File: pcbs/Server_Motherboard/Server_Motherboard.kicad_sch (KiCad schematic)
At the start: 18 parts, among them J1 GSB1C41110SSHR, J2 Conn_01x20, J3 Conn_01x20, U1 ESP32-C3-MINI-1-H4X

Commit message: moving imported parts from my global dir to within this repo
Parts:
- added IC21: DRV8210DRLR, SOTFL50P160X60-6N, symbol SamacSys_Parts:DRV8210DRLR
- added U2: MCP23S17_ML, Package_DFN_QFN:QFN-28-1EP_6x6mm_P0.65mm_EP4.25x4.25mm, symbol Interface_Expansion:MCP23S17_ML
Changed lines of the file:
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@@
+    )
+  )
+  (symbol (lib_id "Interface_Expansion:MCP23S17_ML") (at 250.19 153.67 0) (unit 1)
+    (in_bom yes) (on_board yes) (dnp no) (fields_autoplaced)
+    (property "Reference" "U2" (at 252.3841 125.73 0)
+      (effects (font (size 1.27 1.27)) (justify left))
+    )
+    (property "Value" "MCP23S17_ML" (at 252.3841 128.27 0)
+      (effects (font (size 1.27 1.27)) (justify left))
+    )
+    (property "Footprint" "Package_DFN_QFN:QFN-28-1EP_6x6mm_P0.65mm_EP4.25x4.25mm" (at 255.27 179.07 0)
+      (effects (font (size 1.27 1.27)) (justify left) hide)
+    )
+    (property "Datasheet" "http://ww1.microchip.com/downloads/en/DeviceDoc/20001952C.pdf" (at 255.27 181.61 0)
+      (effects (font (size 1.27 1.27)) (justify left) hide)
+    )
+    (pin "15")
+    (pin "27")
+    (pin "7")
+    (pin "12")
+    (pin "3")
+    (pin "26")
+    (pin "10")
+    (pin "18")
+    (pin "25")
+    (pin "1")
+    (pin "13")
+    (pin "16")
+    (pin "14")
+    (pin "22")
+    (pin "28")
+    (pin "6")
+    (pin "8")
+    (pin "24")
+    (pin "11")
+    (pin "20")
+    (pin "2")
+    (pin "21")
+    (pin "29")
+    (pin "23")
+    (pin "4")
+    (pin "9")
+    (pin "5")
+    (pin "17")
+    (pin "19")
+    (instances
+      (project "Server_Motherboard"
+        (path "/2e2729a6-36ba-49a4-8404-024e36daa1b6"
+          (reference "U2") (unit 1)
+        )
+      )
     )
   )
@@
         )
       )
+    )
+  )
+  (symbol (lib_id "SamacSys_Parts:DRV8210DRLR") (at 189.23 144.78 0) (unit 1)
+    (in_bom yes) (on_board yes) (dnp no) (fields_autoplaced)
+    (property "Reference" "IC21" (at 203.2 137.16 0)
+      (effects (font (size 1.27 1.27)))
+    )
+    (property "Value" "DRV8210DRLR" (at 203.2 139.7 0)
+      (effects (font (size 1.27 1.27)))
+    )
+    (property "Footprint" "SOTFL50P160X60-6N" (at 213.36 142.24 0)
+      (effects (font (size 1.27 1.27)) (justify left) hide)
+    )
+    (property "Datasheet" "https://www.ti.com/lit/ds/symlink/drv8210.pdf?ts=1641207817417&ref_url=https%253A%252F%252Fwww.google.com%252F" (at 213.36 144.78 0)
+      (effects (font (size 1.27 1.27)) (justify left) hide)
+    )
+    (property "Description" "Motor / Motion / Ignition Controllers & Drivers 12-V, 1.76-A brushed DC motor driver with auto sleep mode" (at 213.36 147.32 0)
+      (effects (font (size 1.27 1.27)) (justify left) hide)
+    )
+    (property "Height" "0.6" (at 213.36 149.86 0)
+      (effects (font (size 1.27 1.27)) (justify left) hide)
+    )
+    (property "Mouser Part Number" "595-DRV8210DRLR" (at 213.36 152.4 0)
+      (effects (font (size 1.27 1.27)) (justify left) hide)
+    )
+    (property "Mouser Price/Stock" "https://www.mouser.co.uk/ProductDetail/Texas-Instruments/DRV8210DRLR?qs=7D1LtPJG0i1B1CHsXZuruQ%3D%3D" (at 213.36 154.94 0)
+      (effects (font (size 1.27 1.27)) (justify left) hide)
+    )
+    (property "Manufacturer_Name" "Texas Instruments" (at 213.36 157.48 0)
+      (effects (font (size 1.27 1.27)) (justify left) hide)
+    )
+    (property "Manufacturer_Part_Number" "DRV8210DRLR" (at 213.36 160.02 0)
+      (effects (font (size 1.27 1.27)) (justify left) hide)
+    )
+    (pin "4")
+    (pin "5")
+    (pin "1")
+    (pin "3")
+    (pin "6")
+    (pin "2")
+    (instances
+      (project "Server_Motherboard"
+        (path "/2e2729a6-36ba-49a4-8404-024e36daa1b6"
+          (reference "IC21") (unit 1)
+        )
+      )

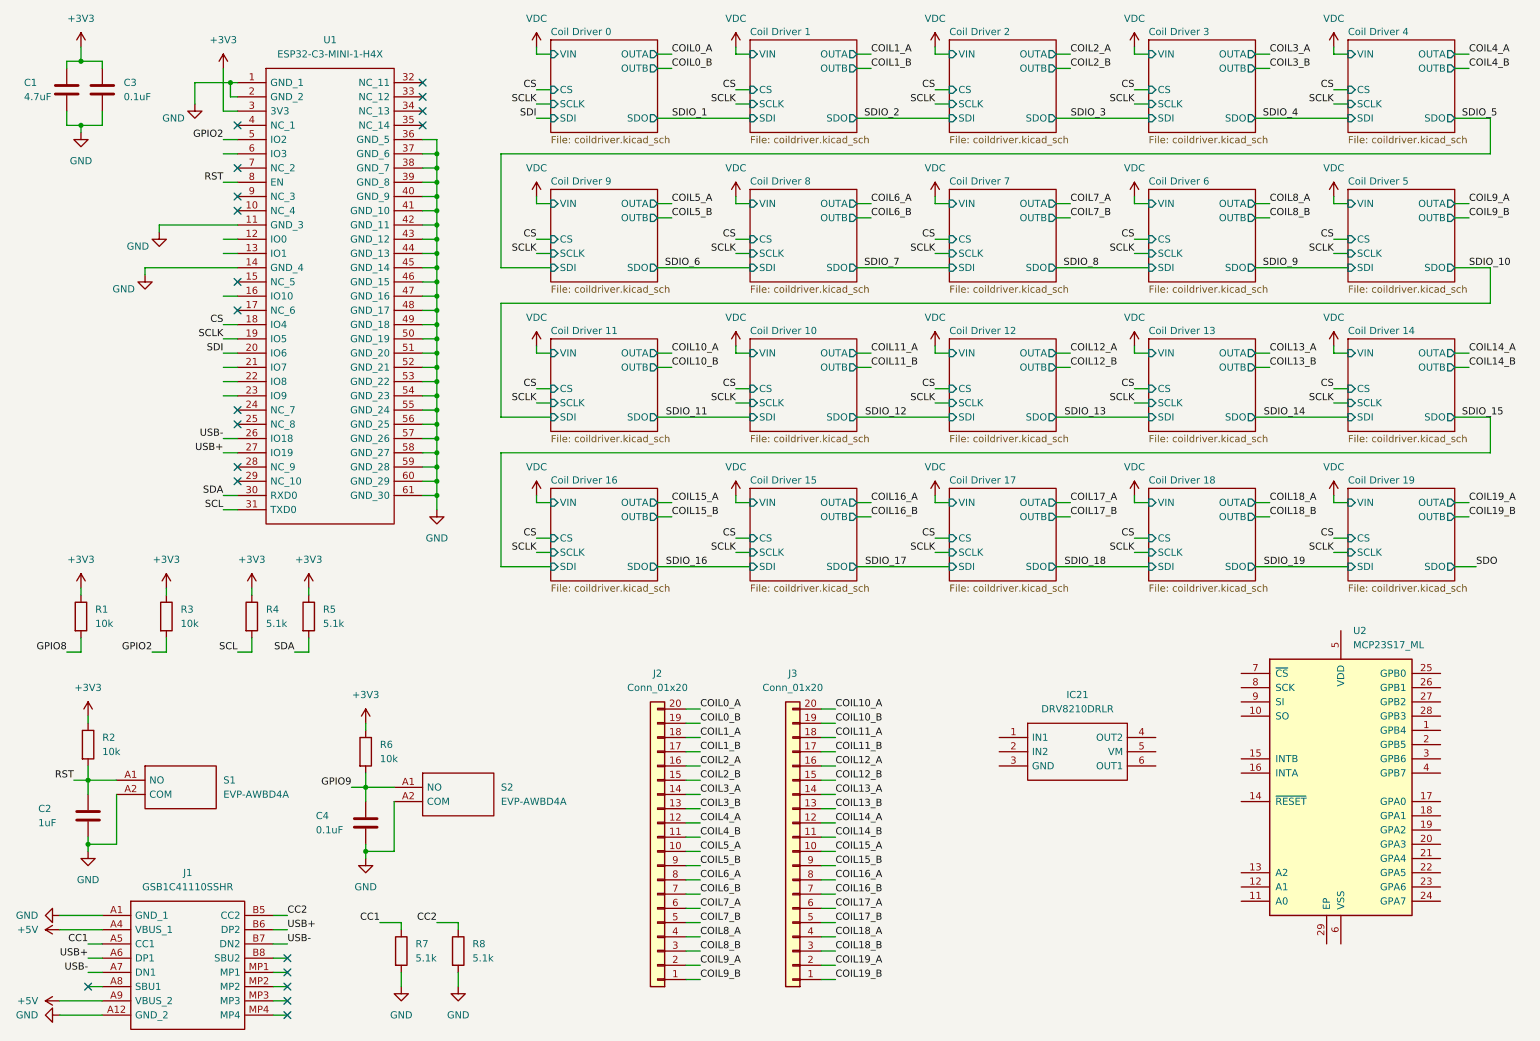
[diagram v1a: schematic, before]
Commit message: mostly finished server pcb, added pogo charge pins to bots, started charge case pcb
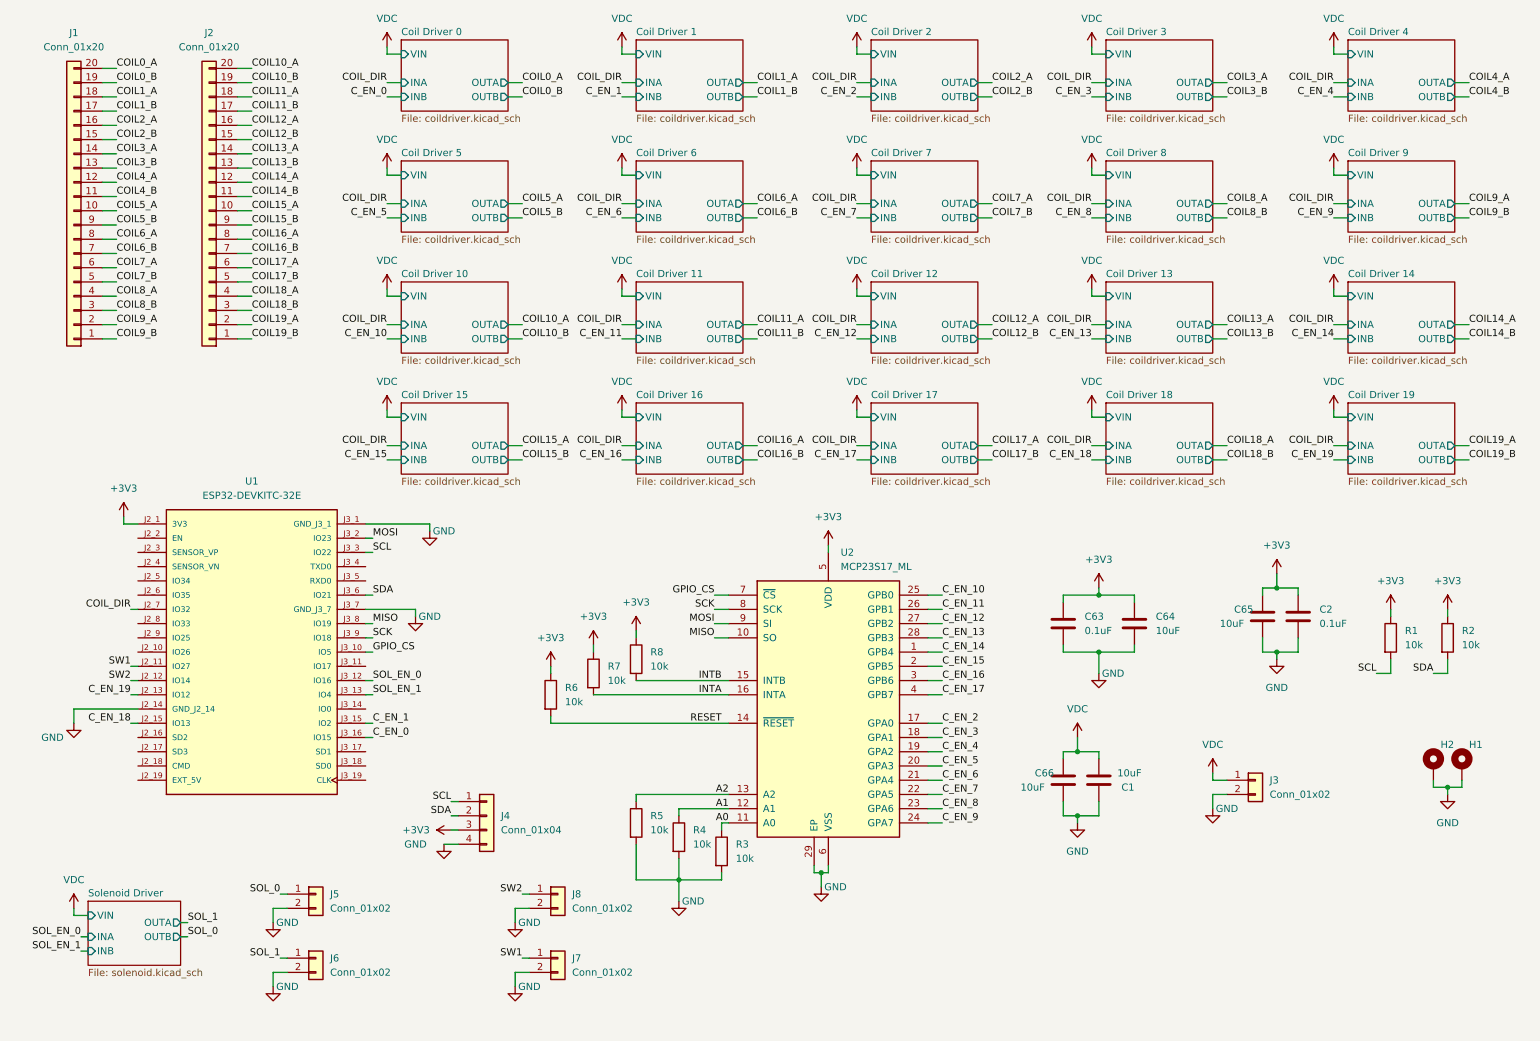
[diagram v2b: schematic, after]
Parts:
- removed C2: 1uF, Capacitor_SMD:C_0402_1005Metric, symbol Device:C
- removed C4: 0.1uF, Capacitor_SMD:C_0402_1005Metric, symbol Device:C
- removed IC21: DRV8210DRLR, SOTFL50P160X60-6N, symbol SamacSys_Parts:DRV8210DRLR
- removed J1: GSB1C41110SSHR, GSB1C41110SSHR, symbol SamacSys_Parts:GSB1C41110SSHR
- removed R1, R2: 10k, Resistor_SMD:R_0402_1005Metric, symbol Device:R
- removed S1, S2: EVP-AWBD4A, EVPAWBD4A, symbol SamacSys_Parts:EVP-AWBD4A
- removed U1: ESP32-C3-MINI-1-H4X, ESP32C3MINI1H4X, symbol SamacSys_Parts:ESP32-C3-MINI-1-H4X
- added C63: 0.1uF, Capacitor_SMD:C_0402_1005Metric, symbol Device:C
- added C64, C65, C66: 10uF, Capacitor_SMD:C_0603_1608Metric, symbol Device:C
- added H1, H2: MountingHole_Pad, MountingHole:MountingHole_2.7mm_M2.5_Pad_TopBottom, symbol Mechanical:MountingHole_Pad
- added J3: Conn_01x02, Connector_PinHeader_2.54mm:PinHeader_1x02_P2.54mm_Vertical, symbol Connector_Generic:Conn_01x02
- added J4: Conn_01x04, Connector_PinHeader_2.54mm:PinHeader_1x04_P2.54mm_Vertical, symbol Connector_Generic:Conn_01x04
- added J5, J6, J7, J8: Conn_01x02, Connector_PinHeader_2.54mm:PinHeader_1x02_P2.54mm_Horizontal, symbol Connector_Generic:Conn_01x02
- added R4, R5: 10k, Resistor_SMD:R_0402_1005Metric, symbol Device:R
- added U1: ESP32-DEVKITC-32E, minibot:MODULE_ESP32-DEVKITC-32E, symbol ESP32-DEVKITC-32E:ESP32-DEVKITC-32E
- C1: value 4.7uF -> 10uF; footprint Capacitor_SMD:C_0402_1005Metric -> Capacitor_SMD:C_0603_1608Metric
- J1: renamed from J2; footprint (none) -> Connector_PinHeader_2.00mm:PinHeader_1x20_P2.00mm_Vertical
- J2: renamed from J3; footprint (none) -> Connector_PinHeader_2.00mm:PinHeader_1x20_P2.00mm_Vertical
- R1: renamed from R4; value 5.1k -> 10k
- R2: renamed from R5; value 5.1k -> 10k
- R7, R8: value 5.1k -> 10k
- renumbered C3 to C2
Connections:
- net CC1 is gone; now on net +3V3: R7.1
- net CC2 is gone; now on net +3V3: R8.1
- net GPIO2 is gone; now on net GND: R3.2
- net GPIO9 is gone; now on net RESET: R6.2
- net +3V3: now also U2.5 (VDD), C63.1, C64.1, C65.1, J4.3 (Pin_3), U1.J2_1 (3V3); no longer C1.2, R3.1
- net GND: now also U2.29 (EP), U2.6 (VSS), C63.2, C64.2, C65.2, C66.2, H1.1, H2.1, J3.2 (Pin_2), J4.4 (Pin_4), J5.2 (Pin_2), J6.2 (Pin_2), J7.2 (Pin_2), J8.2 (Pin_2), R4.2, R5.2, U1.J2_14 (GND_J2_14), U1.J3_1 (GND_J3_1), U1.J3_7 (GND_J3_7); no longer R7.2, R8.2
- net SCL: now also J4.1 (Pin_1), U1.J3_3 (IO22)
- net SDA: now also J4.2 (Pin_2), U1.J3_6 (IO21)
- net VDC: now also C1.2, C66.1, J3.1 (Pin_1)
- net C_EN_14: now reaches U2.1 (GPB4)
- net MISO: now reaches U2.10 (SO)
- net MISO: now also U1.J3_8 (IO19)
- net A0: now reaches U2.11 (A0)
- net A0: now also R3.1
- net A1: now reaches U2.12 (A1)
- net A1: now also R4.1
- net A2: now reaches U2.13 (A2)
- net A2: now also R5.1
- net RESET: now reaches U2.14 (~{RESET})
- net INTB: now reaches U2.15 (INTB)
- net INTB: now also R8.2
- net INTA: now reaches U2.16 (INTA)
- net INTA: now also R7.2
- net C_EN_2: now reaches U2.17 (GPA0)
- net C_EN_3: now reaches U2.18 (GPA1)
- net C_EN_4: now reaches U2.19 (GPA2)
- net C_EN_15: now reaches U2.2 (GPB5)
- net C_EN_5: now reaches U2.20 (GPA3)
- net C_EN_6: now reaches U2.21 (GPA4)
- net C_EN_7: now reaches U2.22 (GPA5)
- net C_EN_8: now reaches U2.23 (GPA6)
- net C_EN_9: now reaches U2.24 (GPA7)
- net C_EN_10: now reaches U2.25 (GPB0)
- net C_EN_11: now reaches U2.26 (GPB1)
- net C_EN_12: now reaches U2.27 (GPB2)
- net C_EN_13: now reaches U2.28 (GPB3)
- net C_EN_16: now reaches U2.3 (GPB6)
- net C_EN_17: now reaches U2.4 (GPB7)
- net GPIO_CS: now reaches U2.7 (~{CS})
- net GPIO_CS: now also U1.J3_10 (IO5)
- net SCK: now reaches U2.8 (SCK)
- net SCK: now also U1.J3_9 (IO18)
- net MOSI: now reaches U2.9 (SI)
- net MOSI: now also U1.J3_2 (IO23)
- new net COIL_DIR: U1.J2_7 (IO32)
- new net C_EN_0: U1.J3_16 (IO15)
- new net C_EN_1: U1.J3_15 (IO2)
- new net C_EN_18: U1.J2_15 (IO13)
- new net C_EN_19: U1.J2_13 (IO12)
- new net SOL_0: J5.1 (Pin_1)
- new net SOL_1: J6.1 (Pin_1)
- new net SOL_EN_0: U1.J3_12 (IO16)
- new net SOL_EN_1: U1.J3_13 (IO4)
- new net SW1: J7.1 (Pin_1), U1.J2_11 (IO27)
- new net SW2: J8.1 (Pin_1), U1.J2_12 (IO14)
- no-connect marks 20 -> 0
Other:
- added sheet Solenoid Driver (solenoid.kicad_sch)
- sheet Coil Driver 0 ports: added INA, INB; removed CS, SCLK, SDI, SDO
- sheet Coil Driver 1 ports: added INA, INB; removed CS, SCLK, SDI, SDO
- sheet Coil Driver 10 ports: added INA, INB; removed CS, SCLK, SDI, SDO
- sheet Coil Driver 11 ports: added INA, INB; removed CS, SCLK, SDI, SDO
- sheet Coil Driver 12 ports: added INA, INB; removed CS, SCLK, SDI, SDO
- sheet Coil Driver 13 ports: added INA, INB; removed CS, SCLK, SDI, SDO
- sheet Coil Driver 14 ports: added INA, INB; removed CS, SCLK, SDI, SDO
- sheet Coil Driver 15 ports: added INA, INB; removed CS, SCLK, SDI, SDO
- sheet Coil Driver 16 ports: added INA, INB; removed CS, SCLK, SDI, SDO
- sheet Coil Driver 17 ports: added INA, INB; removed CS, SCLK, SDI, SDO
- sheet Coil Driver 18 ports: added INA, INB; removed CS, SCLK, SDI, SDO
- sheet Coil Driver 19 ports: added INA, INB; removed CS, SCLK, SDI, SDO
- sheet Coil Driver 2 ports: added INA, INB; removed CS, SCLK, SDI, SDO
- sheet Coil Driver 3 ports: added INA, INB; removed CS, SCLK, SDI, SDO
- sheet Coil Driver 4 ports: added INA, INB; removed CS, SCLK, SDI, SDO
- sheet Coil Driver 5 ports: added INA, INB; removed CS, SCLK, SDI, SDO
- sheet Coil Driver 6 ports: added INA, INB; removed CS, SCLK, SDI, SDO
- sheet Coil Driver 7 ports: added INA, INB; removed CS, SCLK, SDI, SDO
- sheet Coil Driver 8 ports: added INA, INB; removed CS, SCLK, SDI, SDO
- sheet Coil Driver 9 ports: added INA, INB; removed CS, SCLK, SDI, SDO
- moved on the sheet: C2, J1, J2, R1, R2, U2
